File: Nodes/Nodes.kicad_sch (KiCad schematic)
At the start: 8 parts, among them J1 Conn_01x04, J2 Conn_01x04, J3 Conn_01x18, J4 Conn_01x18, J5 Conn_01x18, J6 Conn_01x18

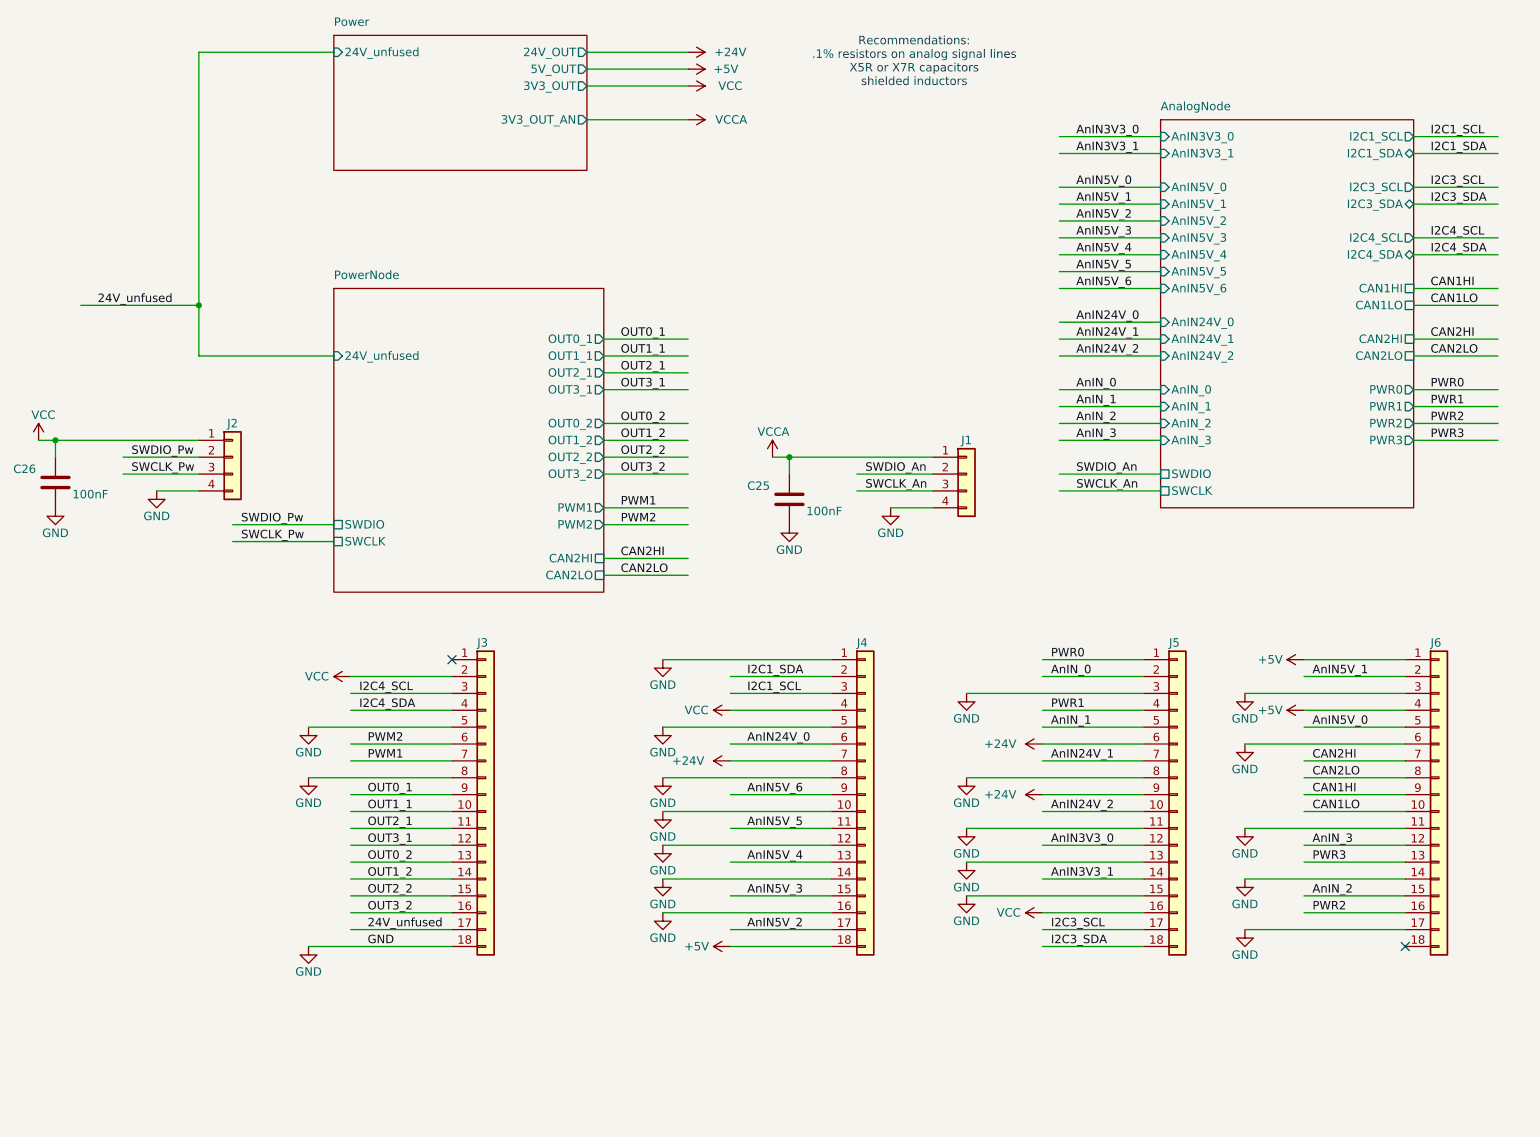
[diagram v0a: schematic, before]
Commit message: Nodes v2.1.2 Improved
- Improved schematic design
- Added two 4.7 uF caps according to the datasheets of the microchips
- Other small changes
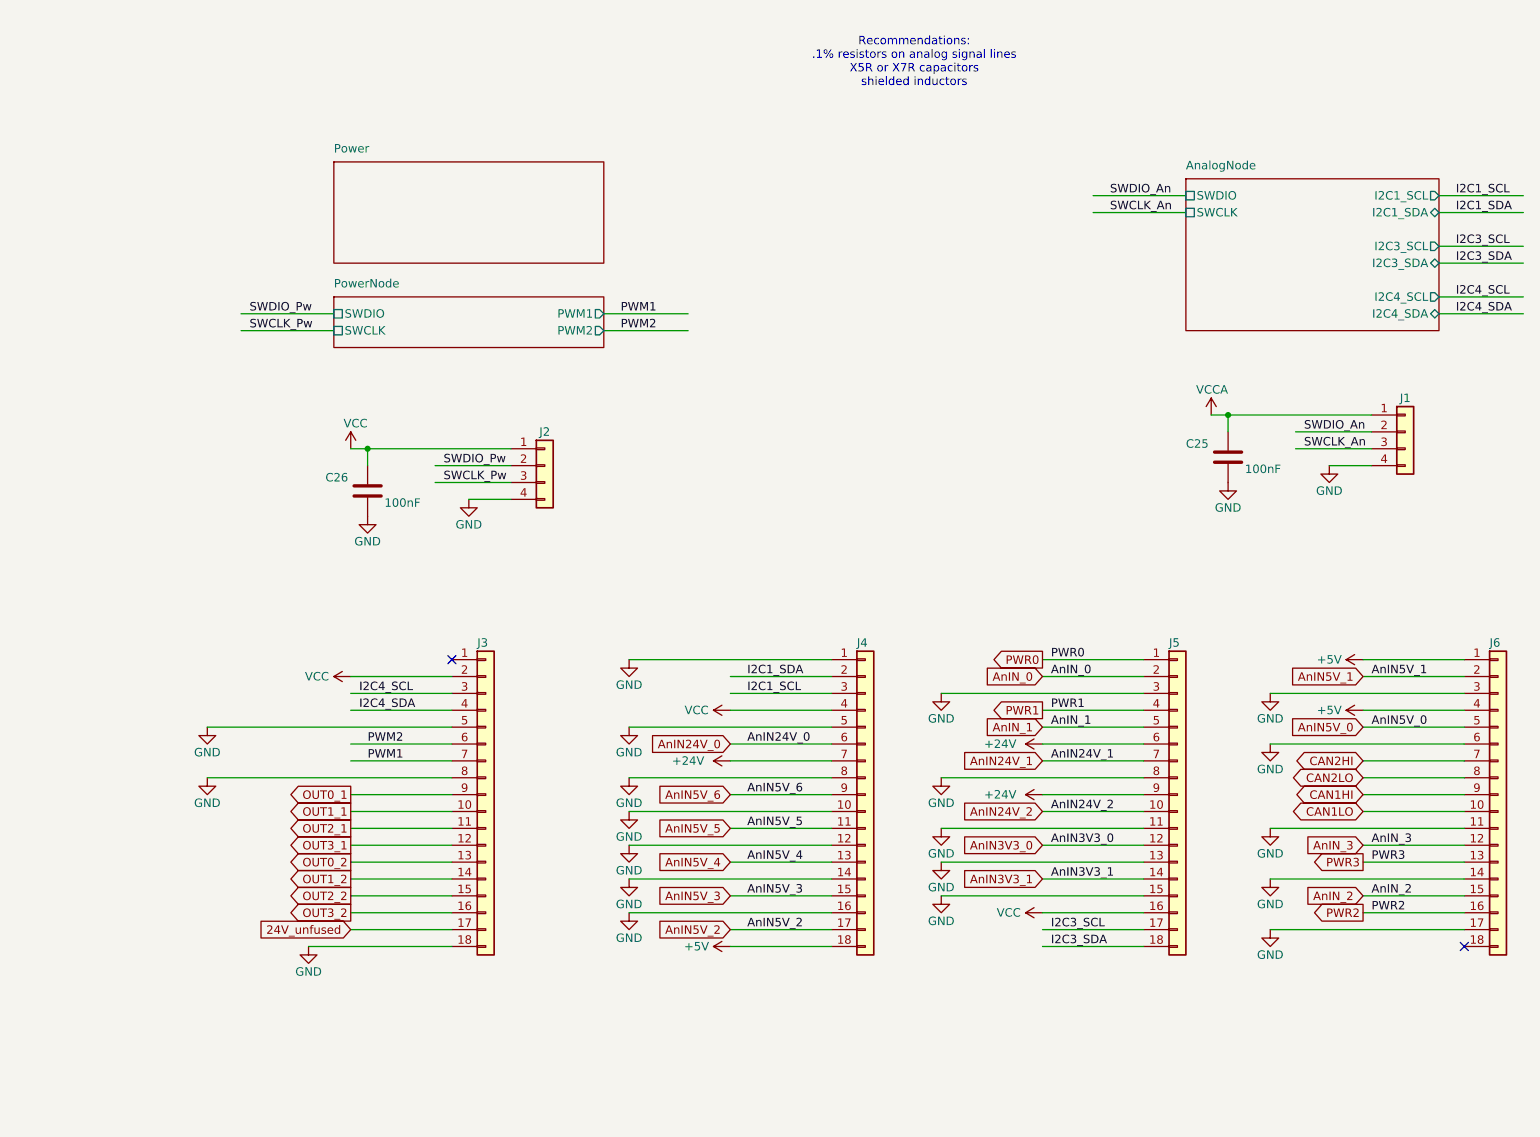
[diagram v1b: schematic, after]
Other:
- sheet AnalogNode ports: added none; removed AnIN24V_0, AnIN24V_1, AnIN24V_2, AnIN3V3_0, AnIN3V3_1, AnIN5V_0, AnIN5V_1, AnIN5V_2, AnIN5V_3, AnIN5V_4, AnIN5V_5, AnIN5V_6, AnIN_0, AnIN_1, AnIN_2, AnIN_3, CAN1HI, CAN1LO, CAN2HI, CAN2LO, PWR0, PWR1, PWR2, PWR3
- sheet Power ports: added none; removed 24V_OUT, 24V_unfused, 3V3_OUT, 3V3_OUT_AN, 5V_OUT
- sheet PowerNode ports: added none; removed 24V_unfused, CAN2HI, CAN2LO, OUT0_1, OUT0_2, OUT1_1, OUT1_2, OUT2_1, OUT2_2, OUT3_1, OUT3_2
- moved on the sheet: C25, C26, J1, J2, J6

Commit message: Nodes v2.2
- This version not compatible with BOB v.2.1.2 and older!
- Completely new layout design
- New power supply system with new voltage regulators
- New microchip STM32G431RBTx for the Analog Node
- New connection system (instead of 18 pin headers now 8 pin and pins were grouped by functions)
- Reduced size of the board by 5%
- Removed power switch for the Analog Node (because this functionality is now provided by a separate voltage regulator. for a more stable voltage)
- Removable ground from the holes added
- Layer numbers added
- Small improvements of the components information were made
- New oscillator for the Nodes
- Removed CAN1, so now only one CAN connection due to the capabilities of the new microchip
- Other small changes and fixes on the schematic and design
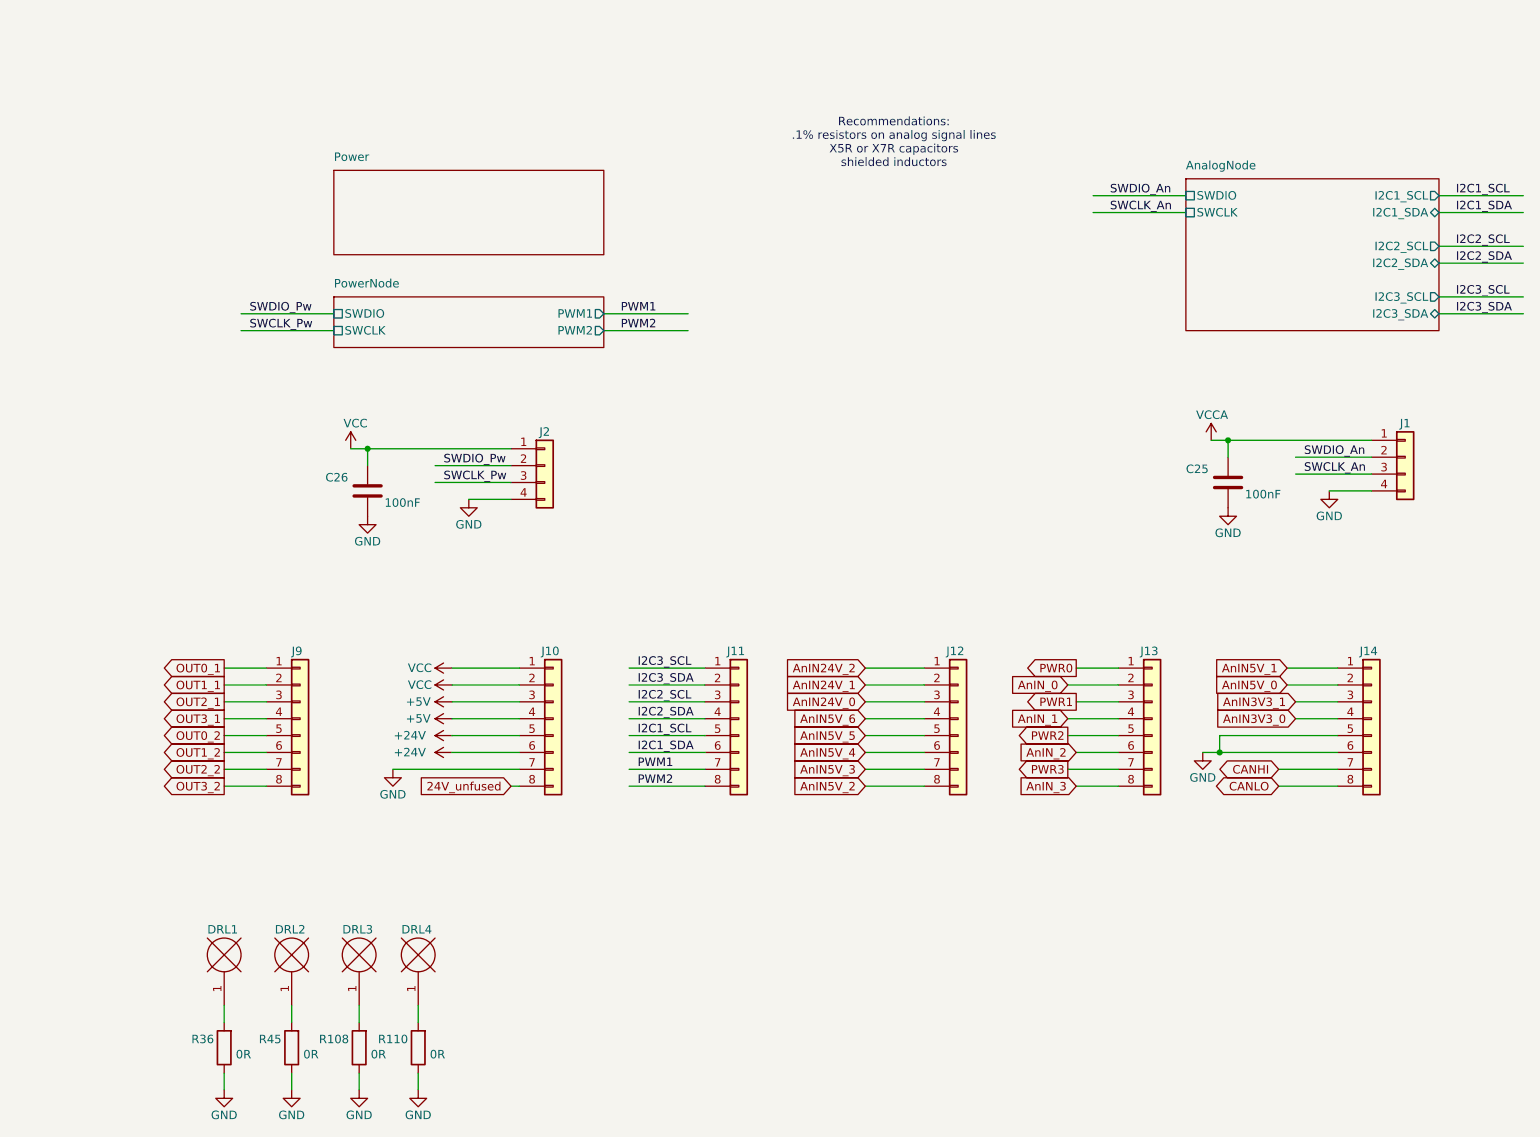
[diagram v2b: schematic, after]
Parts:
- removed J3, J4, J5, J6: Conn_01x18, Connector_PinHeader_2.54mm:PinHeader_1x18_P2.54mm_Vertical, symbol Connector_Generic:Conn_01x18
- added DRL1, DRL2, DRL3, DRL4: HOLE4.28.4, MountingHole:MountingHole_4.3mm_M4_Pad, symbol motorsport_MCU-rescue:HOLE4.28.4-general
- added J10, J11, J12, J13, J14, J9: Conn_01x08, Connector_PinHeader_2.54mm:PinHeader_1x08_P2.54mm_Vertical, symbol Connector_Generic:Conn_01x08
- added R108, R110, R36, R45: 0R, Resistor_SMD:R_0805_2012Metric_Pad1.20x1.40mm_HandSolder, symbol Device:R
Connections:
- net +24V: now also J10.5 (Pin_5), J10.6 (Pin_6)
- net +5V: now also J10.3 (Pin_3), J10.4 (Pin_4)
- net 24V_unfused: now also J10.8 (Pin_8)
- net AnIN24V_0: now also J12.3 (Pin_3)
- net AnIN24V_1: now also J12.2 (Pin_2)
- net AnIN24V_2: now also J12.1 (Pin_1)
- net AnIN3V3_0: now also J14.4 (Pin_4)
- net AnIN3V3_1: now also J14.3 (Pin_3)
- net AnIN5V_0: now also J14.2 (Pin_2)
- net AnIN5V_1: now also J14.1 (Pin_1)
- net AnIN5V_2: now also J12.8 (Pin_8)
- net AnIN5V_3: now also J12.7 (Pin_7)
- net AnIN5V_4: now also J12.6 (Pin_6)
- net AnIN5V_5: now also J12.5 (Pin_5)
- net AnIN5V_6: now also J12.4 (Pin_4)
- net AnIN_0: now also J13.2 (Pin_2)
- net AnIN_1: now also J13.4 (Pin_4)
- net AnIN_2: now also J13.6 (Pin_6)
- net AnIN_3: now also J13.8 (Pin_8)
- net GND: now also J10.7 (Pin_7), J14.5 (Pin_5), J14.6 (Pin_6), R108.1, R110.1, R36.1, R45.1
- net I2C1_SCL: now also J11.5 (Pin_5)
- net I2C1_SDA: now also J11.6 (Pin_6)
- net I2C3_SCL: now also J11.1 (Pin_1)
- net I2C3_SDA: now also J11.2 (Pin_2)
- net OUT0_1: now also J9.1 (Pin_1)
- net OUT0_2: now also J9.5 (Pin_5)
- net OUT1_1: now also J9.2 (Pin_2)
- net OUT1_2: now also J9.6 (Pin_6)
- net OUT2_1: now also J9.3 (Pin_3)
- net OUT2_2: now also J9.7 (Pin_7)
- net OUT3_1: now also J9.4 (Pin_4)
- net OUT3_2: now also J9.8 (Pin_8)
- net PWM1: now also J11.7 (Pin_7)
- net PWM2: now also J11.8 (Pin_8)
- net PWR0: now also J13.1 (Pin_1)
- net PWR1: now also J13.3 (Pin_3)
- net PWR2: now also J13.5 (Pin_5)
- net PWR3: now also J13.7 (Pin_7)
- net VCC: now also J10.1 (Pin_1), J10.2 (Pin_2)
- new net: DRL2.1, R45.2
- new net: DRL1.1, R36.2
- new net: DRL4.1, R110.2
- new net: DRL3.1, R108.2
- new net CANHI: J14.7 (Pin_7)
- new net CANLO: J14.8 (Pin_8)
- new net I2C2_SCL: J11.3 (Pin_3)
- new net I2C2_SDA: J11.4 (Pin_4)
- no-connect marks 2 -> 0
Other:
- sheet AnalogNode ports: added I2C2_SCL, I2C2_SDA; removed I2C4_SCL, I2C4_SDA
- moved on the sheet: C25, J1

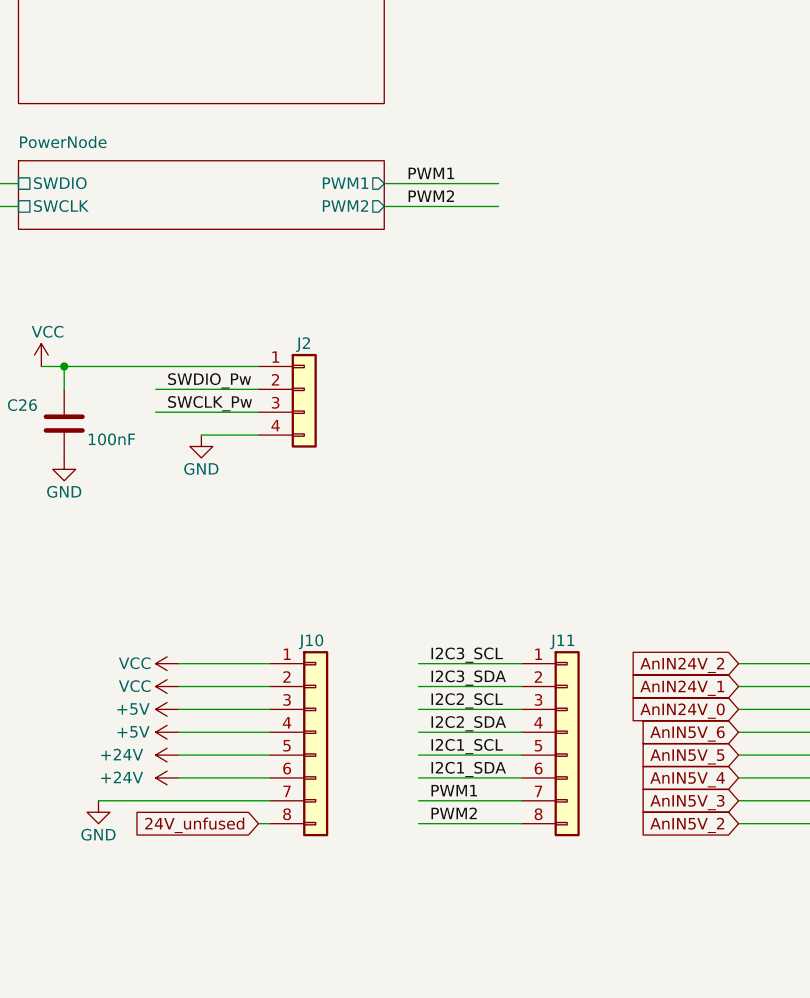
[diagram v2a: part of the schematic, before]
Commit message: Nodes v2.2.2
- Level-Shifter on PWM1 for 24V applications added
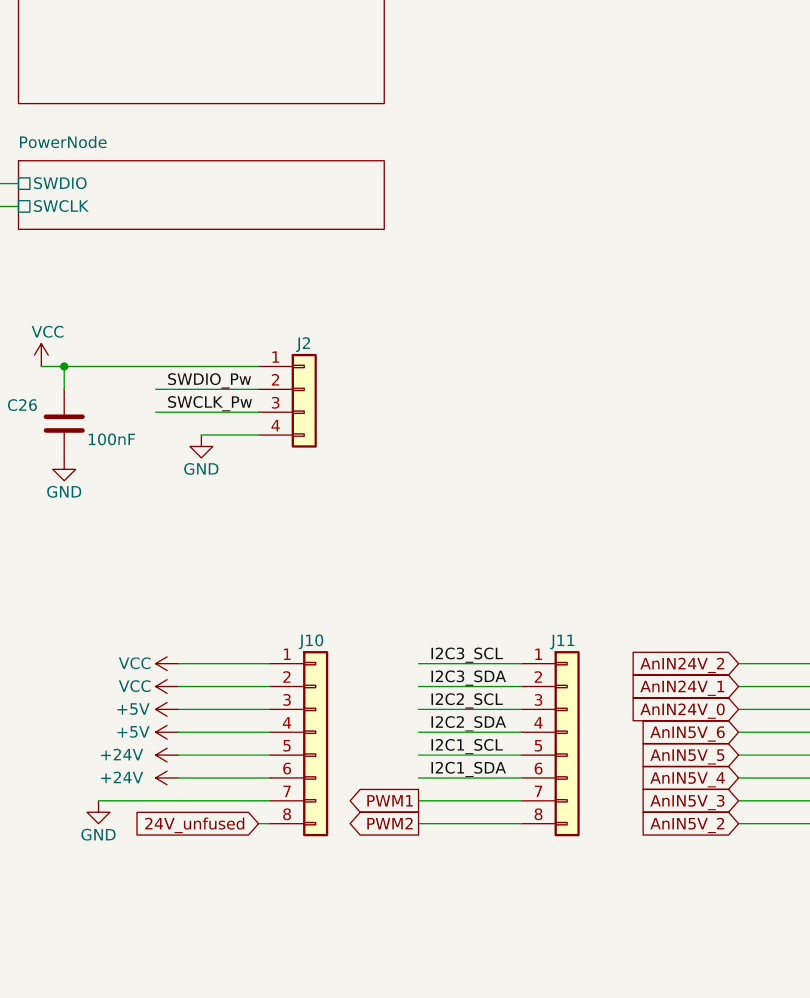
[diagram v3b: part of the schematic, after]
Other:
- sheet PowerNode ports: added none; removed PWM1, PWM2
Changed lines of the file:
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@@
 	(wire
 		(pts
-			(xy 104.14 63.5) (xy 116.84 63.5)
-		)
-		(stroke
-			(width 0)
-			(type default)
-		)
-	)
-	(wire
-		(pts
 			(xy 219.71 87.63) (xy 213.36 87.63)
 		)
@@
 	(wire
 		(pts
-			(xy 104.14 60.96) (xy 116.84 60.96)
-		)
-		(stroke
-			(width 0)
-			(type default)
-		)
-	)
-	(wire
-		(pts
 			(xy 175.26 114.3) (xy 181.61 114.3)
 		)
@@
 		)
 	)
-	(label "PWM1"
-		(at 106.68 60.96 0)
-		(fields_autoplaced yes)
-		(effects
-			(font
-				(size 1.27 1.27)
-			)
-			(justify left bottom)
-		)
-	)
 	(label "I2C1_SDA"
 		(at 232.41 45.72 0)
@@
 		)
 	)
-	(label "PWM1"
-		(at 109.22 129.54 0)
-		(fields_autoplaced yes)
-		(effects
-			(font
-				(size 1.27 1.27)
-			)
-			(justify left bottom)
-		)
-	)
 	(label "I2C3_SDA"
 		(at 232.41 60.96 0)
@@
 		)
 	)
-	(label "PWM2"
-		(at 106.68 63.5 0)
-		(fields_autoplaced yes)
-		(effects
-			(font
-				(size 1.27 1.27)
-			)
-			(justify left bottom)
-		)
-	)
 	(label "SWCLK_An"
 		(at 180.34 45.72 0)
@@
 		)
 	)
-	(label "PWM2"
-		(at 109.22 132.08 0)
-		(fields_autoplaced yes)
-		(effects
-			(font
-				(size 1.27 1.27)
-			)
-			(justify left bottom)
-		)
-	)
 	(global_label "PWR3"
 		(shape output)
@@
 		)
 	)
+	(global_label "PWM1"
+		(shape output)
+		(at 107.95 129.54 180)
+		(fields_autoplaced yes)
+		(effects
+			(font
+				(size 1.27 1.27)
+			)
+			(justify right)
+		)
+		(property "Intersheetrefs" "${INTERSHEET_REFS}"
+			(at 99.5825 129.54 0)
+			(effects
+				(font
+					(size 1.27 1.27)
+				)
+				(justify right)
+				(hide yes)
+			)
+		)
+	)
 	(global_label "OUT0_2"
 		(shape output)
@@
 		)
 	)
+	(global_label "PWM2"
+		(shape output)
+		(at 107.95 132.08 180)
+		(fields_autoplaced yes)
+		(effects
+			(font
+				(size 1.27 1.27)
+			)
+			(justify right)
+		)
+		(property "Intersheetrefs" "${INTERSHEET_REFS}"
+			(at 99.5825 132.08 0)
+			(effects
+				(font
+					(size 1.27 1.27)
+				)
+				(justify right)
+				(hide yes)
+			)
+		)
+	)
 	(global_label "AnIN_1"
 		(shape input)
@@
 			)
 		)
-		(pin "PWM1" output
-			(at 104.14 60.96 0)
-			(effects
-				(font
-					(size 1.27 1.27)
-				)
-				(justify right)
-			)
-		)
-		(pin "PWM2" output
-			(at 104.14 63.5 0)
-			(effects
-				(font
-					(size 1.27 1.27)
-				)
-				(justify right)
-			)
-		)
